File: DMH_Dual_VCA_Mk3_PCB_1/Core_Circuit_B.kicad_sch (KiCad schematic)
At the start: 24 parts, among them Q3 BC548, Q4 BC548, U2 TL074

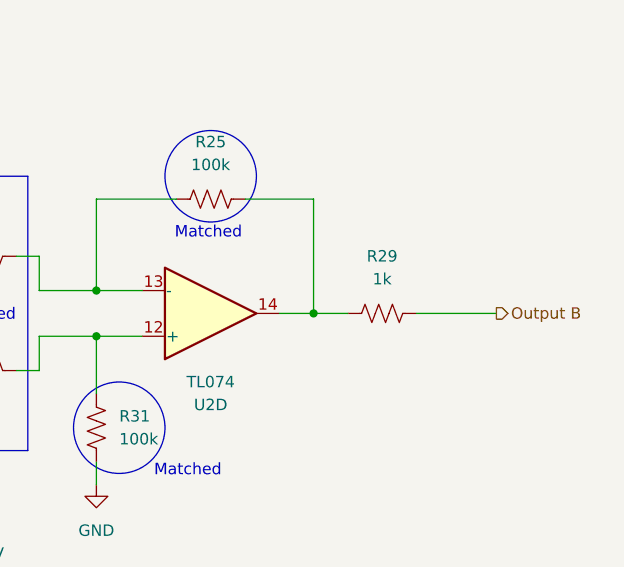
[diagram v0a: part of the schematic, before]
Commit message: 2nd VCA design done
Clipping design in progress
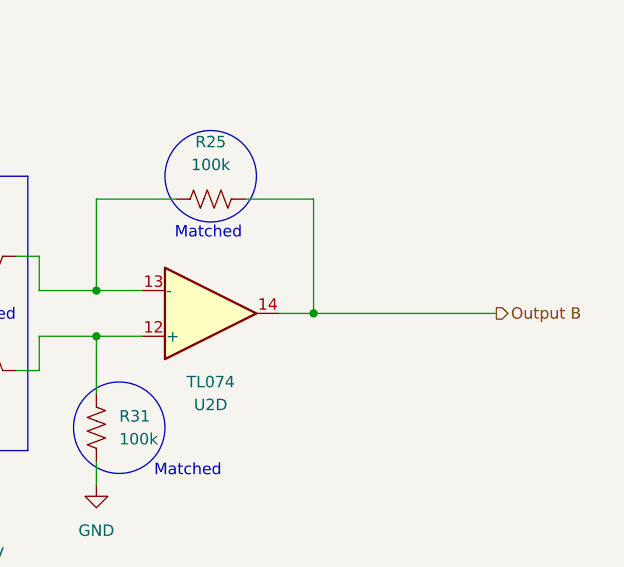
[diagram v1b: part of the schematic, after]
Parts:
- removed R29: 1k, Resistor_THT:R_Axial_DIN0207_L6.3mm_D2.5mm_P7.62mm_Horizontal, symbol Device:R_US
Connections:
- net Output B: now also R25.1, U2.14
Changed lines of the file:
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@@
-	(wire
-		(pts
-			(xy 257.81 50.8) (xy 266.7 50.8)
-		)
-		(stroke
-			(width 0)
-			(type default)
-		)
-	)
 	(wire
 		(pts
@@
 	(wire
 		(pts
-			(xy 246.38 50.8) (xy 250.19 50.8)
+			(xy 246.38 50.8) (xy 266.7 50.8)
 		)
 		(stroke
@@
 		)
 	)
-	(symbol
-		(lib_id "Device:R_US")
-		(at 254 50.8 270)
-		(unit 1)
-		(exclude_from_sim no)
-		(in_bom yes)
-		(on_board yes)
-		(dnp no)
-		(fields_autoplaced yes)
-		(property "Reference" "R29"
-			(at 254 44.45 90)
-			(effects
-				(font
-					(size 1.27 1.27)
-				)
-			)
-		)
-		(property "Value" "1k"
-			(at 254 46.99 90)
-			(effects
-				(font
-					(size 1.27 1.27)
-				)
-			)
-		)
-		(property "Footprint" "Resistor_THT:R_Axial_DIN0207_L6.3mm_D2.5mm_P7.62mm_Horizontal"
-			(at 253.746 51.816 90)
-			(effects
-				(font
-					(size 1.27 1.27)
-				)
-				(hide yes)
-			)
-		)
-		(property "Datasheet" "~"
-			(at 254 50.8 0)
-			(effects
-				(font
-					(size 1.27 1.27)
-				)
-				(hide yes)
-			)
-		)
-		(property "Description" "Resistor, US symbol"
-			(at 254 50.8 0)
-			(effects
-				(font
-					(size 1.27 1.27)
-				)
-				(hide yes)
-			)
-		)
-		(property "Function" ""
-			(at 254 50.8 0)
-			(effects
-				(font
-					(size 1.27 1.27)
-				)
-			)
-		)
-		(pin "1"
-		)
-		(pin "2"
-		)
-		(instances
-			(project "DMH_Transistor_VCA_PCB"
-				(path "/58f4306d-5387-4983-bb08-41a2313fd315/7915b580-c9b0-4472-ab9c-d9fb99b1a92f"
-					(reference "R29")
-					(unit 1)
-				)
-			)
-		)
-	)
